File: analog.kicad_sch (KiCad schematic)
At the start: 41 parts, among them Q2 AO3400A, U1 TL494, U5 INA180A2, U9 OP07

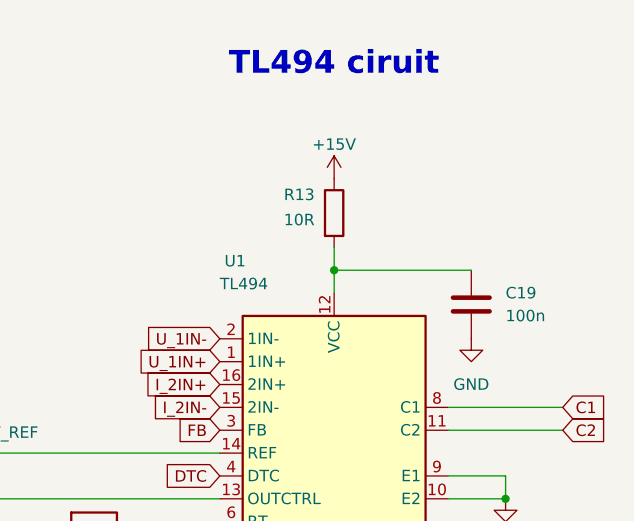
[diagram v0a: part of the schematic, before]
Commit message: fan and temp sensor tracing
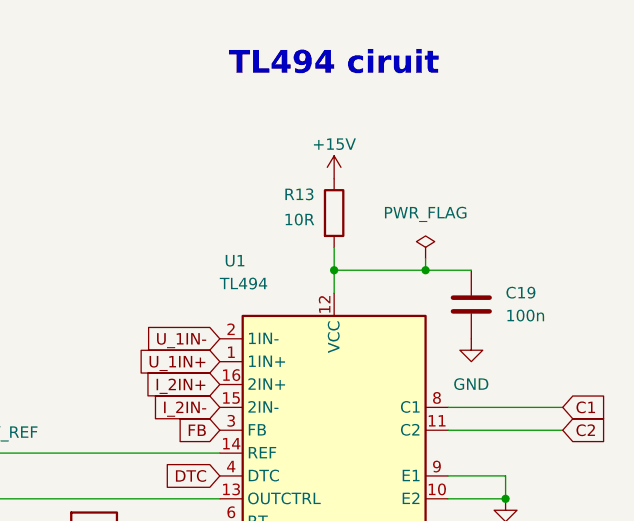
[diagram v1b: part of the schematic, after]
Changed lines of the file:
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@@
+	)
+	(junction
+		(at 261.62 41.91)
+		(diameter 0)
+		(color 0 0 0 0)
 	)
 	(junction
@@
 	(wire
 		(pts
-			(xy 251.46 41.91) (xy 266.7 41.91)
+			(xy 251.46 41.91) (xy 261.62 41.91)
 		)
 		(stroke
@@
 	(wire
 		(pts
+			(xy 261.62 40.64) (xy 261.62 41.91)
+		)
+		(stroke
+			(width 0)
+			(type default)
+		)
+	)
+	(wire
+		(pts
 			(xy 62.23 154.94) (xy 62.23 158.75)
 		)
@@
 		(pts
 			(xy 78.74 27.94) (xy 81.28 27.94)
+		)
+		(stroke
+			(width 0)
+			(type default)
+		)
+	)
+	(wire
+		(pts
+			(xy 261.62 41.91) (xy 266.7 41.91)
 		)
 		(stroke
@@
 					(unit 1)
 				)
+			)
+		)
+	)
+	(symbol
+		(lib_id "power:PWR_FLAG")
+		(at 261.62 40.64 0)
+		(unit 1)
+		(exclude_from_sim no)
+		(in_bom yes)
+		(on_board yes)
+		(dnp no)
+		(fields_autoplaced yes)
+		(property "Reference" "#FLG01"
+			(at 261.62 38.735 0)
+			(effects
+				(font
+					(size 1.27 1.27)
+				)
+				(hide yes)
+			)
+		)
+		(property "Value" "PWR_FLAG"
+			(at 261.62 35.56 0)
+			(effects
+				(font
+					(size 1.27 1.27)
+				)
+			)
+		)
+		(property "Footprint" ""
+			(at 261.62 40.64 0)
+			(effects
+				(font
+					(size 1.27 1.27)
+				)
+				(hide yes)
+			)
+		)
+		(property "Datasheet" "~"
+			(at 261.62 40.64 0)
+			(effects
+				(font
+					(size 1.27 1.27)
+				)
+				(hide yes)
+			)
+		)
+		(property "Description" "Special symbol for telling ERC where power comes from"
+			(at 261.62 40.64 0)
+			(effects
+				(font
+					(size 1.27 1.27)
+				)
+				(hide yes)
+			)
+		)
+		(pin "1"
+		)
+		(instances
+			(project "RPS_ATX"
+				(path "/485c2fed-5176-4ba8-b79d-ac7eddb44491/75639b50-c04a-47dd-b6e6-c8da699a633c"
+					(reference "#FLG01")
+					(unit 1)
+				)

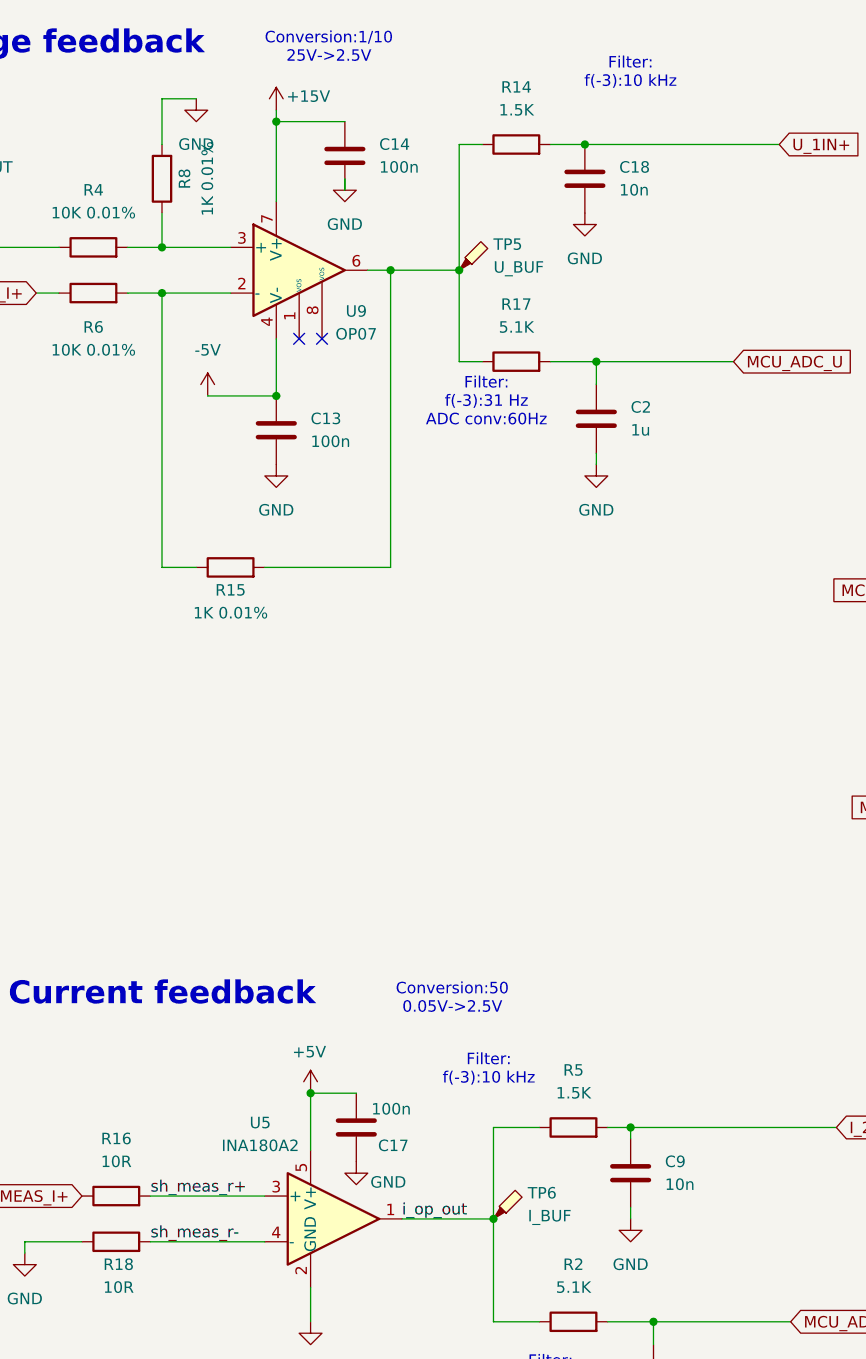
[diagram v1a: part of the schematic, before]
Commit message: minor changes (0805 for 0.1% R, new Y)
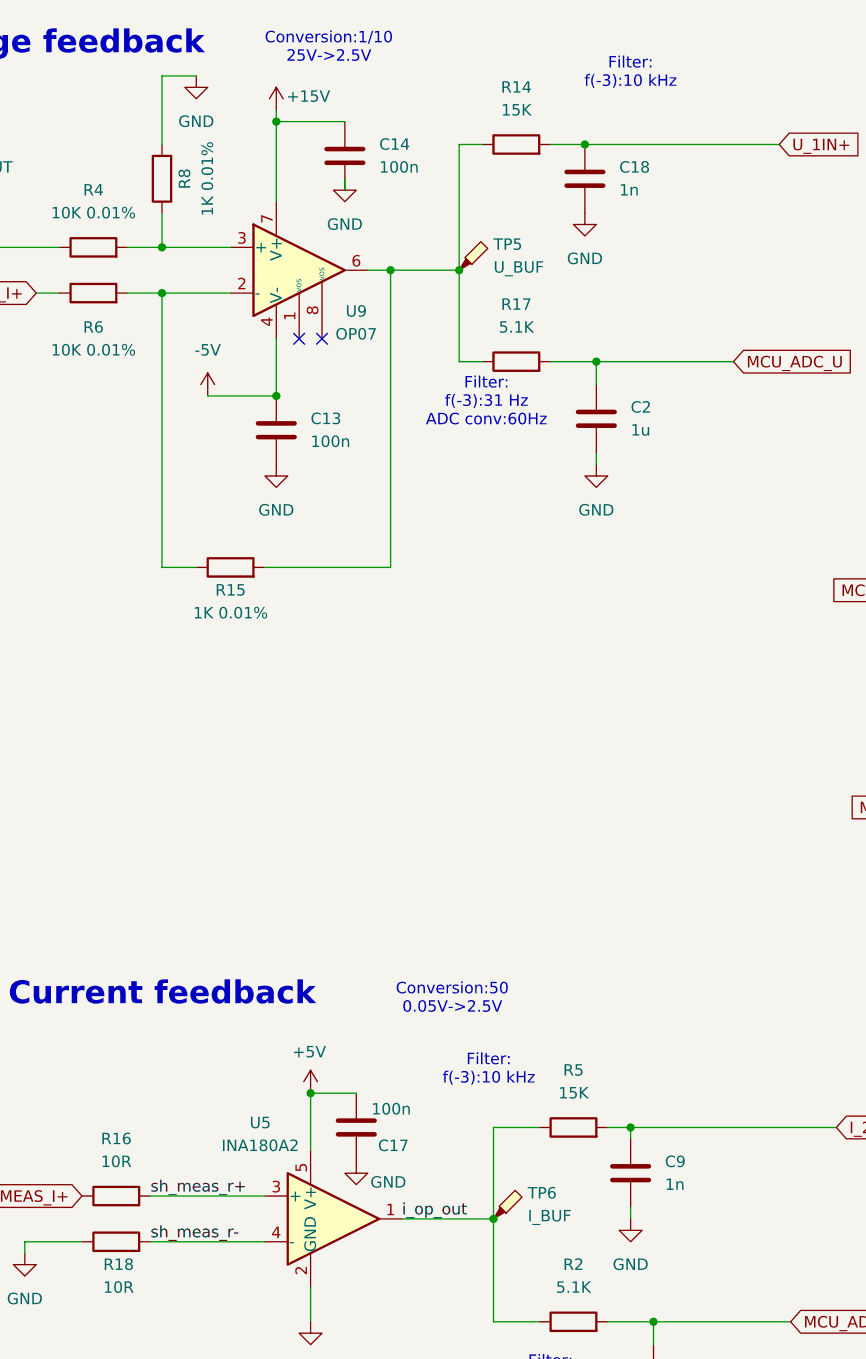
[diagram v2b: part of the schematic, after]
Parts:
- C18, C9: value 10n -> 1n
- R14, R5: value 1.5K -> 15K
- R15, R4, R6, R8: footprint Resistor_SMD:R_1206_3216Metric_Pad1.30x1.75mm_HandSolder -> Resistor_SMD:R_0805_2012Metric_Pad1.20x1.40mm_HandSolder
- TP5, TP6, TP7, TP8, TP9: now left out of the parts list

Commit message: changing concept
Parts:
- removed C2, C7: 1u, Capacitor_SMD:C_1206_3216Metric_Pad1.33x1.80mm_HandSolder, symbol Device:C
- removed R17, R2: 5.1K, Resistor_SMD:R_0805_2012Metric_Pad1.20x1.40mm_HandSolder, symbol Device:R
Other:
- note removed: "Filter: f(-3):31 Hz ADC conv:60Hz"

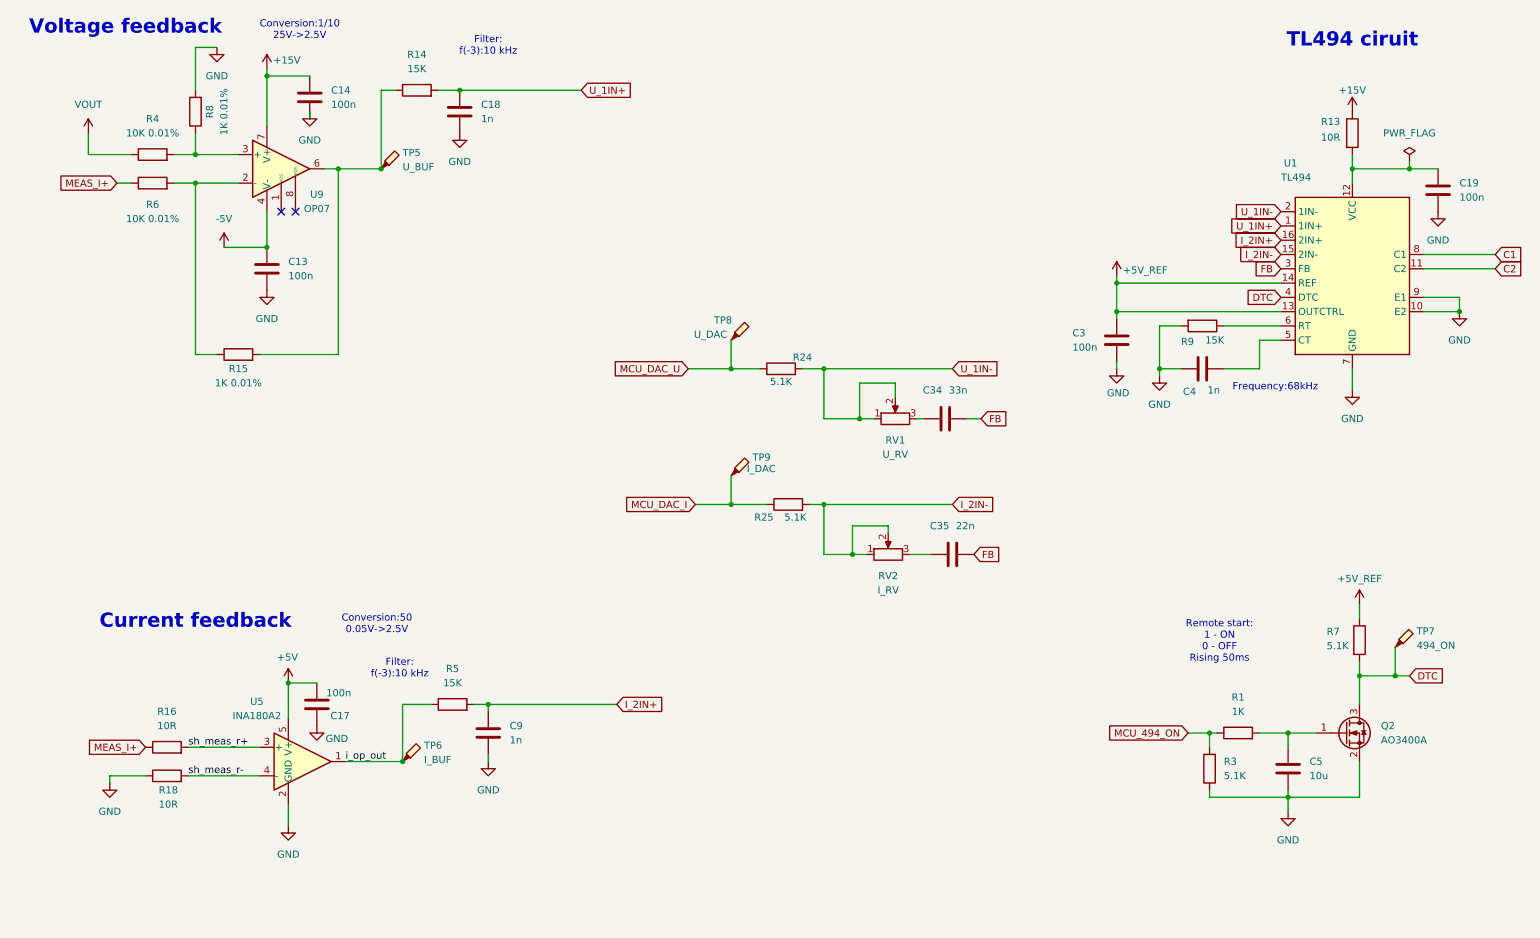
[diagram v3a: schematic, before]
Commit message: excluding STM32G431
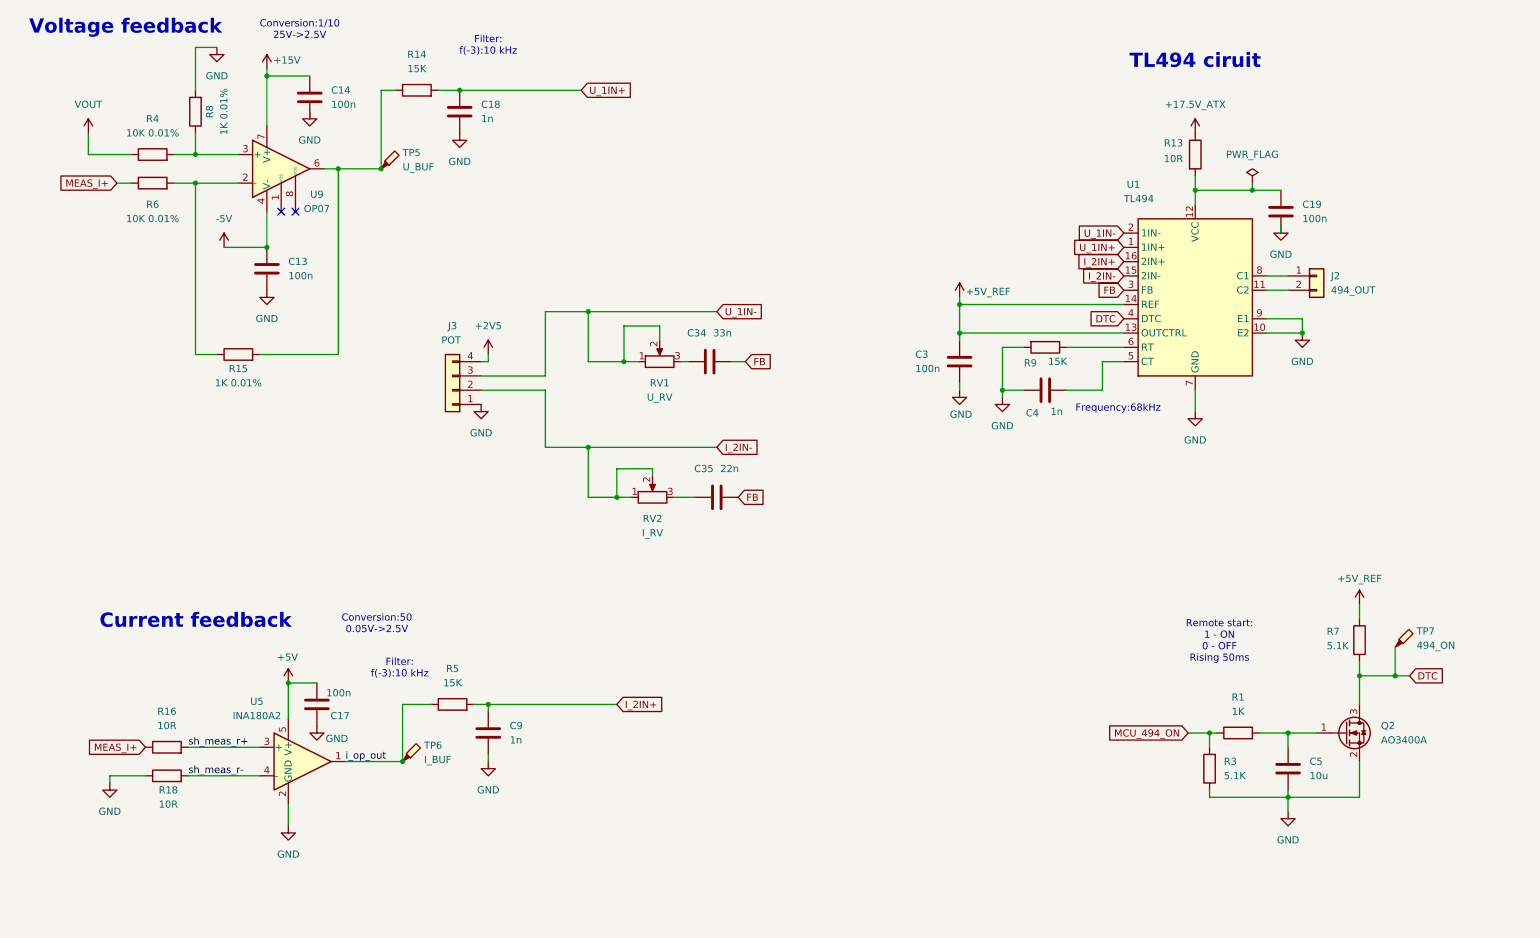
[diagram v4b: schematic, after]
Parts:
- removed R24, R25: 5.1K, Resistor_SMD:R_0805_2012Metric_Pad1.20x1.40mm_HandSolder, symbol Device:R
- removed TP8: U_DAC, TestPoint:TestPoint_Pad_D2.0mm, symbol Connector:TestPoint_Probe
- removed TP9: I_DAC, TestPoint:TestPoint_Pad_D2.0mm, symbol Connector:TestPoint_Probe
- added J2: 494_OUT, Connector_PinHeader_2.54mm:PinHeader_1x02_P2.54mm_Vertical, symbol Connector_Generic:Conn_01x02
- added J3: POT, Connector_PinHeader_2.54mm:PinHeader_1x04_P2.54mm_Vertical, symbol Connector_Generic:Conn_01x04
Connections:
- net +15V: no longer R13.1
- net GND: now also J3.1 (Pin_1)
- net I_2IN-: now also J3.2 (Pin_2)
- net U_1IN-: now also J3.3 (Pin_3)
- net C1: no longer names the net of U1.8 (C1)
- net C1: now also J2.1 (Pin_1)
- net C2: no longer names the net of U1.11 (C2)
- net C2: now also J2.2 (Pin_2)
- new net +17.5V_ATX: R13.1
- new net +2V5: J3.4 (Pin_4)
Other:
- moved on the sheet: C19, C3, C34, C35, C4, R13, R9, RV1, RV2, U1

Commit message: lm358 as U and I meas
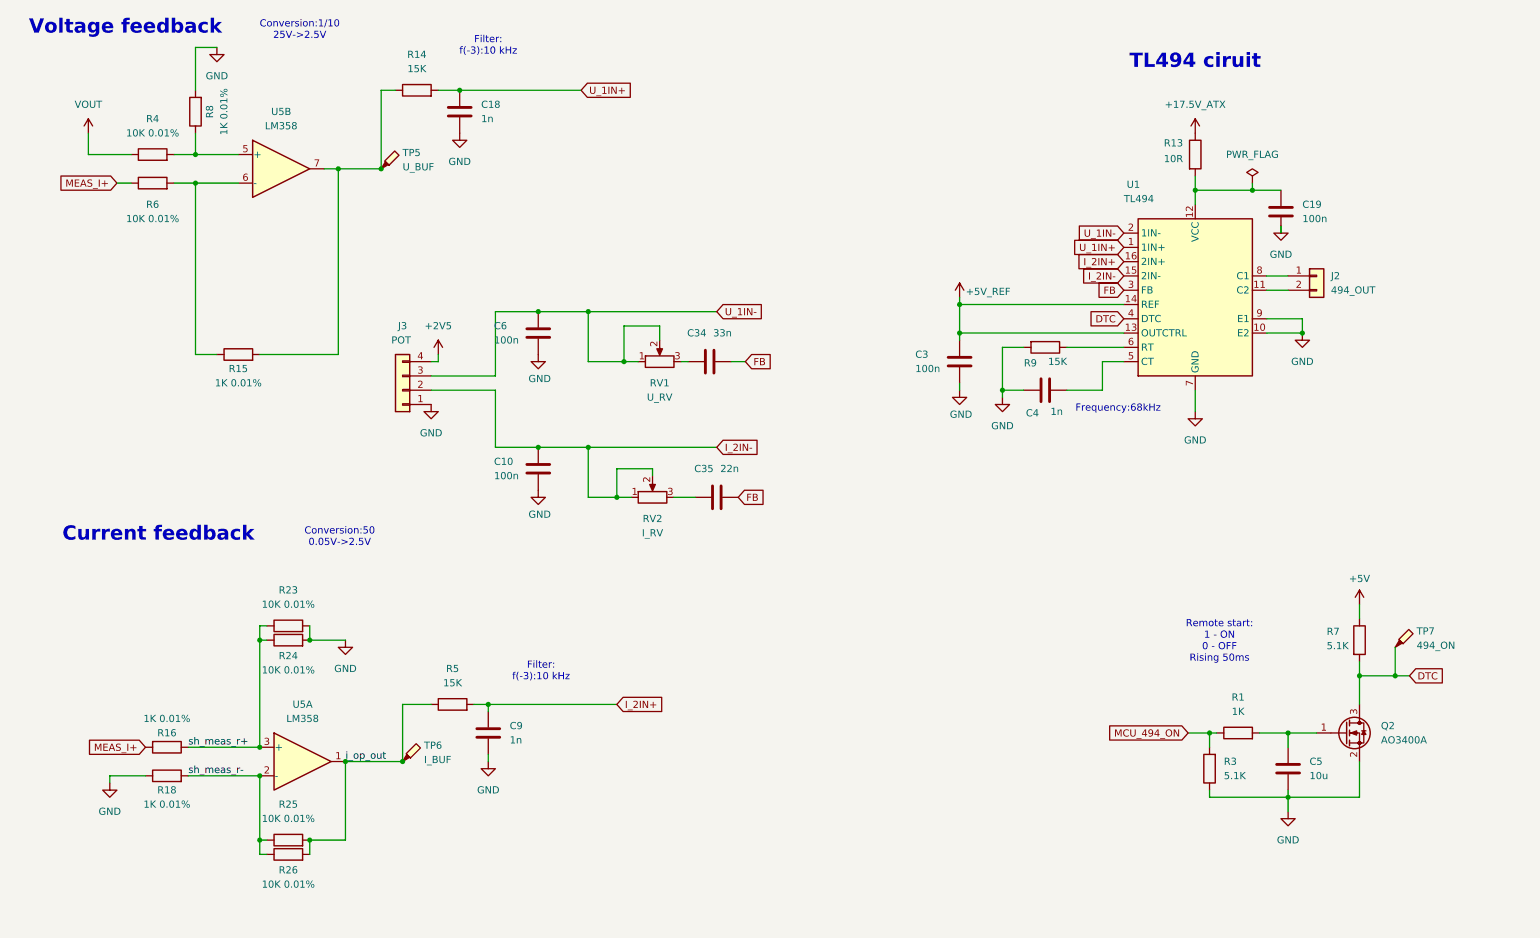
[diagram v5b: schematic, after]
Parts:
- removed C13, C14, C17: 100n, Capacitor_SMD:C_0805_2012Metric_Pad1.18x1.45mm_HandSolder, symbol Device:C
- removed U5: INA180A2, Package_TO_SOT_SMD:SOT-23-5, symbol Amplifier_Current:INA180A2
- removed U9: OP07, Package_SO:SOIC-8_3.9x4.9mm_P1.27mm, symbol Amplifier_Operational:OP07
- added C10, C6: 100n, Capacitor_SMD:C_0805_2012Metric_Pad1.18x1.45mm_HandSolder, symbol Device:C
- added R23, R24, R25, R26: 10K 0.01%, Resistor_SMD:R_0805_2012Metric_Pad1.20x1.40mm_HandSolder, symbol Device:R
- added U5: LM358, Package_SO:SOIC-8_3.9x4.9mm_P1.27mm, symbol Amplifier_Operational:LM358
- R16, R18: value 10R -> 1K 0.01%; footprint Resistor_SMD:R_1206_3216Metric_Pad1.30x1.75mm_HandSolder -> Resistor_SMD:R_0805_2012Metric_Pad1.20x1.40mm_HandSolder
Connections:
- net +5V: now also R7.1
- net +5V_REF: no longer R7.1
- net GND: now also C10.2, C6.2, R23.2, R24.2
- net I_2IN-: now also C10.1
- net MEAS_I+: now also R16.2; no longer R16.1
- net U_1IN-: now also C6.1
- net i_op_out: now also R25.2, R26.2, U5.1
- net sh_meas_r+: now also R16.1, R23.1, R24.1, U5.3 (+); no longer R16.2
- net sh_meas_r-: now also R25.1, R26.1, U5.2 (-)
- net at R15.1, R6.2: now also U5.6 (-)
- net at R4.2, R8.1: now also U5.5 (+)
- net at R14.1, R15.2, TP5.1: now also U5.7
- no-connect marks 2 -> 0
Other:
- moved on the sheet: J3

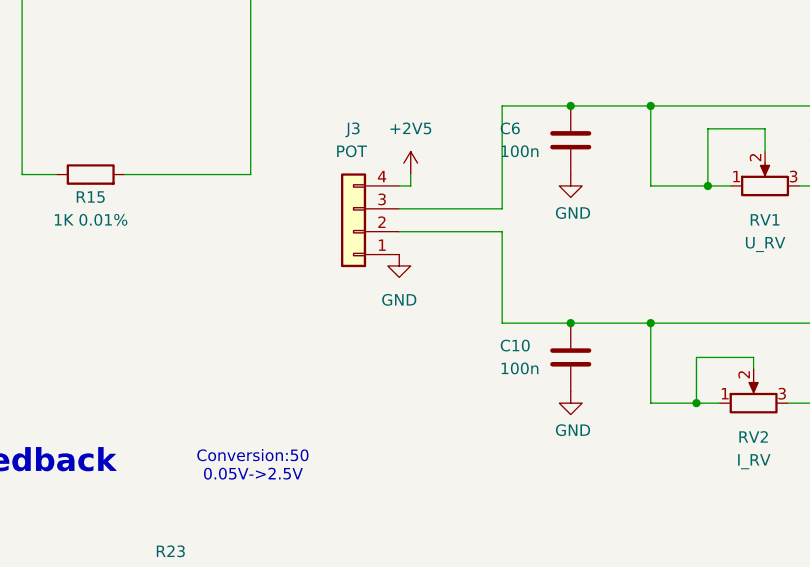
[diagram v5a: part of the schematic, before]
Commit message: added gnd vias, need to isolate power and signal GND
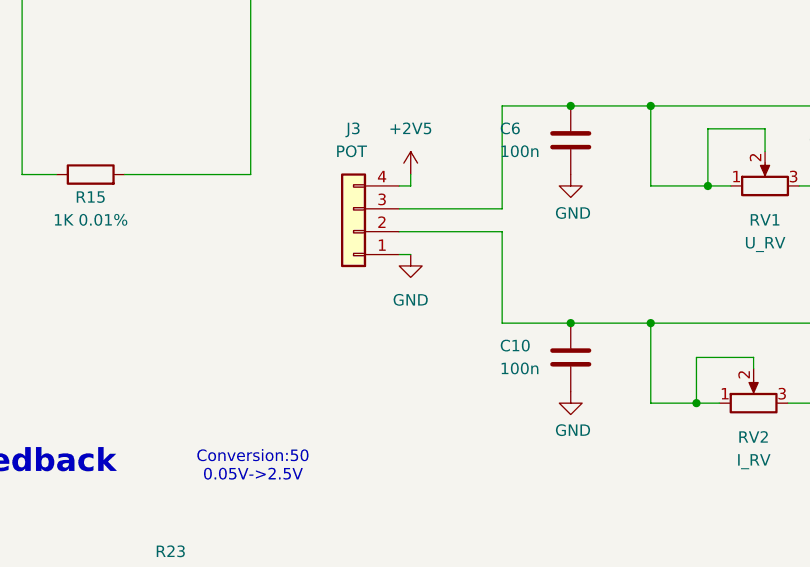
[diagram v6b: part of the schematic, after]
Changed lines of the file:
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@@
 	(wire
 		(pts
+			(xy 88.9 83.82) (xy 87.63 83.82)
+		)
+		(stroke
+			(width 0)
+			(type default)
+		)
+	)
+	(wire
+		(pts
 			(xy 92.71 27.94) (xy 114.3 27.94)
 		)
@@
 	(symbol
 		(lib_id "power:GND")
-		(at 87.63 83.82 0)
+		(at 88.9 83.82 0)
 		(unit 1)
 		(exclude_from_sim no)
@@
 		(fields_autoplaced yes)
 		(property "Reference" "#PWR042"
-			(at 87.63 90.17 0)
+			(at 88.9 90.17 0)
 			(effects
 				(font
@@
 		)
 		(property "Value" "GND"
-			(at 87.63 88.9 0)
+			(at 88.9 88.9 0)
 			(effects
 				(font
@@
 		)
 		(property "Footprint" ""
-			(at 87.63 83.82 0)
+			(at 88.9 83.82 0)
 			(effects
 				(font
@@
 		)
 		(property "Datasheet" ""
-			(at 87.63 83.82 0)
+			(at 88.9 83.82 0)
 			(effects
 				(font
@@
 		)
 		(property "Description" "Power symbol creates a global label with name \"GND\" , ground"
-			(at 87.63 83.82 0)
+			(at 88.9 83.82 0)
 			(effects
 				(font
